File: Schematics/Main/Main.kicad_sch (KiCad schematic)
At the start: 0 parts

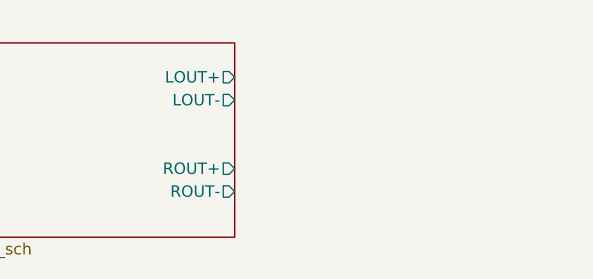
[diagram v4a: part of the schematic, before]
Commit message: Added potentiometer and loudspeakers to audio schematic
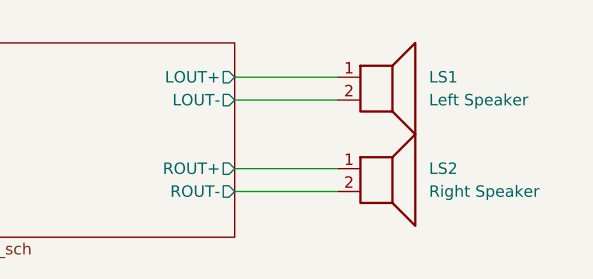
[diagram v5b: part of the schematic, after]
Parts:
- added LS1: Left Speaker, symbol Device:Speaker
- added LS2: Right Speaker, symbol Device:Speaker
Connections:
- net Audiosystem/LOUT+: now also LS1.1
- net Audiosystem/LOUT-: now also LS1.2
- net Audiosystem/ROUT+: now also LS2.1
- net Audiosystem/ROUT-: now also LS2.2
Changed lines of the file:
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@@
 		(date "2025-02-21")
+	)
+	(wire
+		(pts
+			(xy 138.43 130.81) (xy 149.86 130.81)
+		)
+		(stroke
+			(width 0)
+			(type default)
+		)
+	)
+	(wire
+		(pts
+			(xy 138.43 128.27) (xy 149.86 128.27)
+		)
+		(stroke
+			(width 0)
+			(type default)
+		)
+	)
+	(wire
+		(pts
+			(xy 138.43 140.97) (xy 149.86 140.97)
+		)
+		(stroke
+			(width 0)
+			(type default)
+		)
+	)
+	(wire
+		(pts
+			(xy 138.43 138.43) (xy 149.86 138.43)
+		)
+		(stroke
+			(width 0)
+			(type default)
+		)
+	)
+	(symbol
+		(lib_id "Device:Speaker")
+		(at 154.94 128.27 0)
+		(unit 1)
+		(exclude_from_sim no)
+		(in_bom yes)
+		(on_board yes)
+		(dnp no)
+		(fields_autoplaced yes)
+		(property "Reference" "LS1"
+			(at 160.02 128.2699 0)
+			(effects
+				(font
+					(size 1.27 1.27)
+				)
+				(justify left)
+			)
+		)
+		(property "Value" "Left Speaker"
+			(at 160.02 130.8099 0)
+			(effects
+				(font
+					(size 1.27 1.27)
+				)
+				(justify left)
+			)
+		)
+		(property "Footprint" ""
+			(at 154.94 133.35 0)
+			(effects
+				(font
+					(size 1.27 1.27)
+				)
+				(hide yes)
+			)
+		)
+		(property "Datasheet" "~"
+			(at 154.686 129.54 0)
+			(effects
+				(font
+					(size 1.27 1.27)
+				)
+				(hide yes)
+			)
+		)
+		(property "Description" "Speaker"
+			(at 154.94 128.27 0)
+			(effects
+				(font
+					(size 1.27 1.27)
+				)
+				(hide yes)
+			)
+		)
+		(pin "2"
+		)
+		(pin "1"
+		)
+		(instances
+			(project ""
+				(path "/2b6c83b8-b6db-46e9-a845-f7ffa0649aa2"
+					(reference "LS1")
+					(unit 1)
+				)
+			)
+		)
+	)
+	(symbol
+		(lib_id "Device:Speaker")
+		(at 154.94 138.43 0)
+		(unit 1)
+		(exclude_from_sim no)
+		(in_bom yes)
+		(on_board yes)
+		(dnp no)
+		(fields_autoplaced yes)
+		(property "Reference" "LS2"
+			(at 160.02 138.4299 0)
+			(effects
+				(font
+					(size 1.27 1.27)
+				)
+				(justify left)
+			)
+		)
+		(property "Value" "Right Speaker"
+			(at 160.02 140.9699 0)
+			(effects
+				(font
+					(size 1.27 1.27)
+				)
+				(justify left)
+			)
+		)
+		(property "Footprint" ""
+			(at 154.94 143.51 0)
+			(effects
+				(font
+					(size 1.27 1.27)
+				)
+				(hide yes)
+			)
+		)
+		(property "Datasheet" "~"
+			(at 154.686 139.7 0)
+			(effects
+				(font
+					(size 1.27 1.27)
+				)
+				(hide yes)
+			)
+		)
+		(property "Description" "Speaker"
+			(at 154.94 138.43 0)
+			(effects
+				(font
+					(size 1.27 1.27)
+				)
+				(hide yes)
+			)
+		)
+		(pin "2"
+		)
+		(pin "1"
+		)
+		(instances
+			(project ""
+				(path "/2b6c83b8-b6db-46e9-a845-f7ffa0649aa2"
+					(reference "LS2")
+					(unit 1)
+				)
+			)
+		)
 	)
 	(sheet
